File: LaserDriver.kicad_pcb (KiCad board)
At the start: 2 copper layers, 40.2 x 40.5 mm, 31 parts, among them J100 Screw_Terminal_01x04, J101 Screw_Terminal_01x02, J102 nano_left, J103 nano_right, U100 TPS92513DGQR

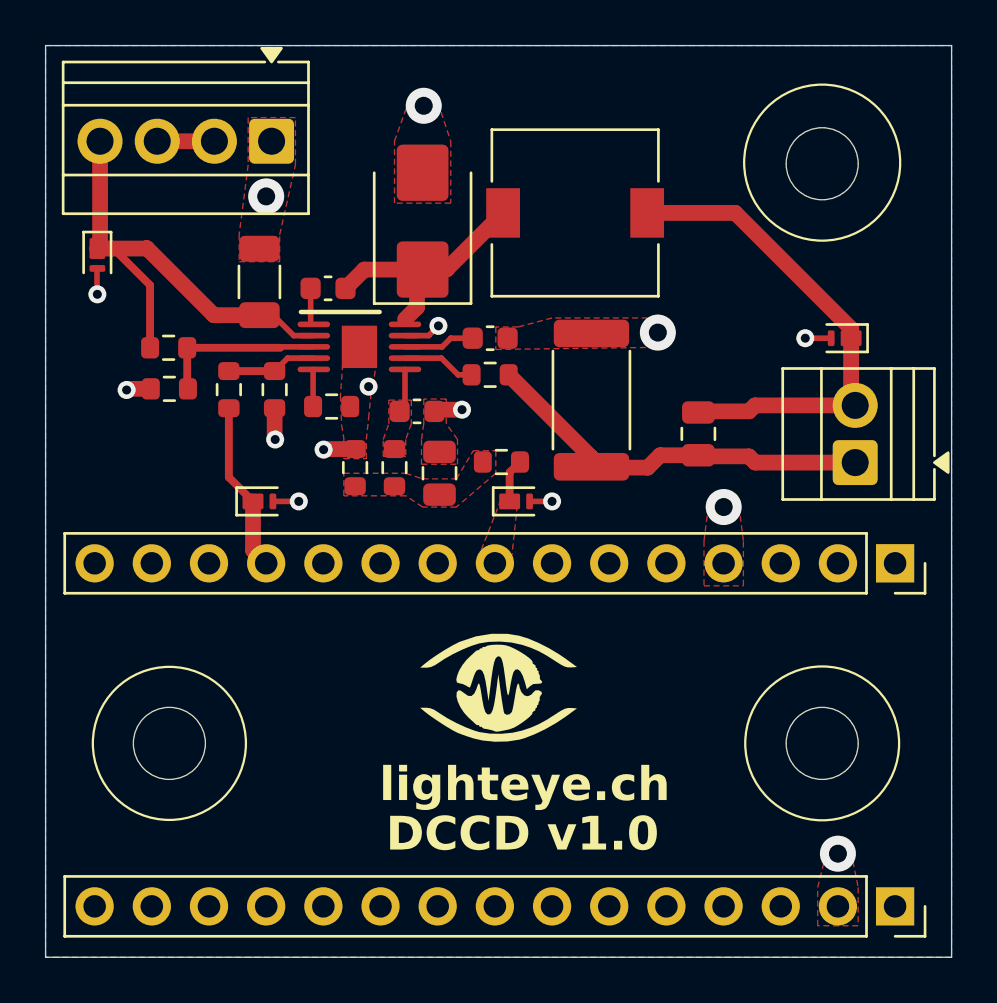
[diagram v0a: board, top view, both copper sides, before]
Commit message: increased screw size, fixed dimensions
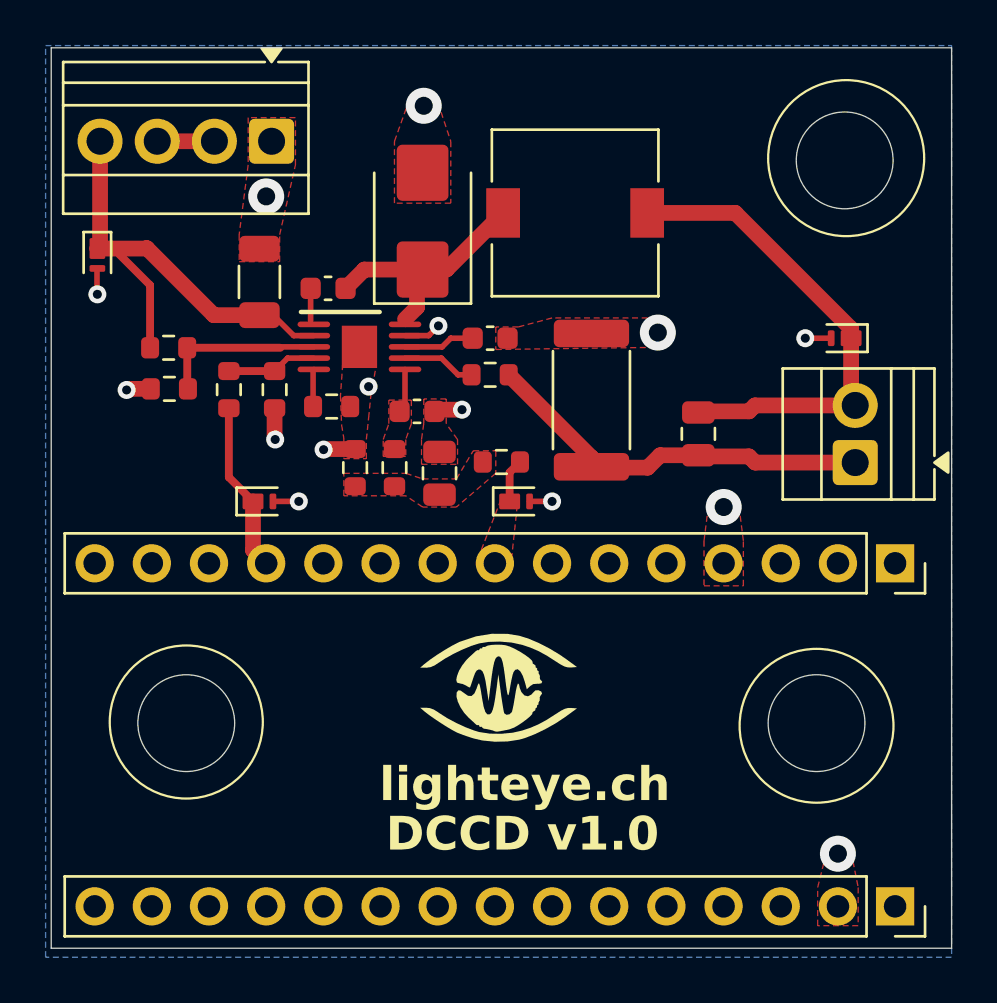
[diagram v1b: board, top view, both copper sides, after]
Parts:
- H1, H2, H3: footprint MountingHole:MountingHole_3.2mm_M3 -> MountingHole:MountingHole_4.3mm_M4
- moved H1 1.17 mm to (35.8, 127.1)
- moved H2 1.01 mm to (65.0, 102.1)
- moved H3 0.93 mm to (63.8, 127.1)
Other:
- board size 40.2 x 40.5 mm -> 40 x 40 mm

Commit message: fine changes
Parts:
- removed H2: MountingHole, MountingHole:MountingHole_4.3mm_M4
- moved J101 14.3 mm to (64.5, 101.3), turned to 180 degrees
- moved D102 10.1 mm to (58.5, 102.2), turned to -90 degrees
- moved C104 9.09 mm to (63.2, 106.5), turned to 0 degrees
- moved R105 2.06 mm to (55.8, 113.2), turned to -90 degrees
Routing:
- net Net-(D102-K): track 21.8 -> 12.8 mm
- net Net-(J101-Pin_1): track 18.1 -> 22.0 mm
- net GND: track 12.8 -> 13.9 mm
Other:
- board text added: "LightEye"
- board text removed: "lighteye.ch"

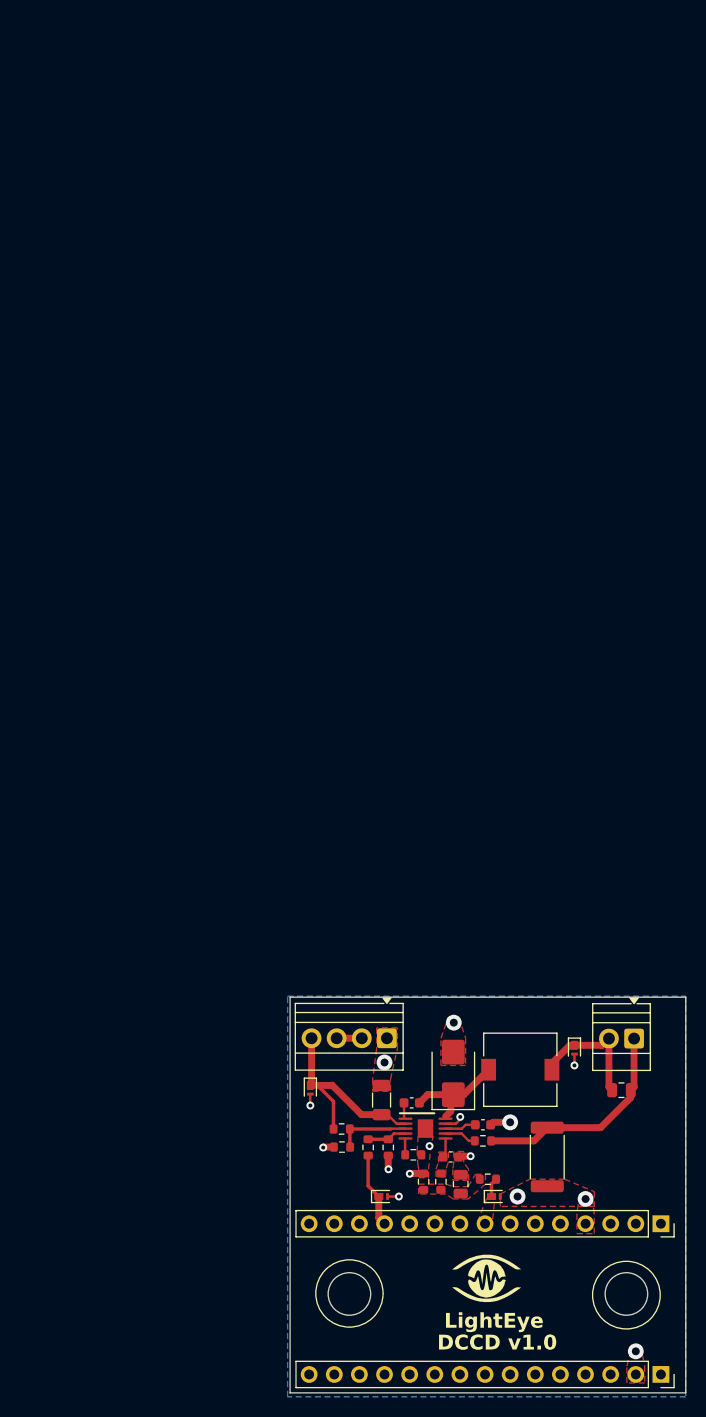
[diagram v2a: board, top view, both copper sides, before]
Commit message: Fixed supplier and manufacturer issues
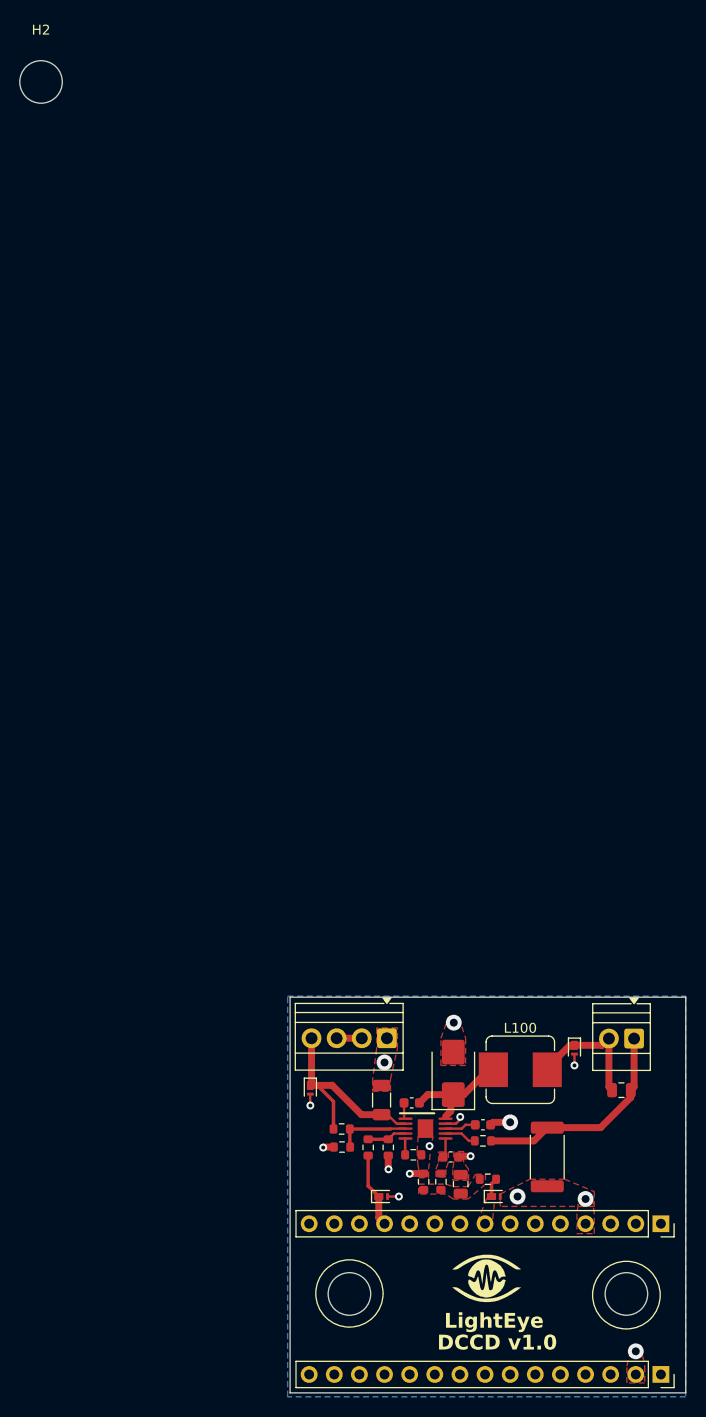
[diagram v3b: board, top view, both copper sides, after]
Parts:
- added H2: MountingHole, MountingHole:MountingHole_4.3mm_M4, F.Cu at (4.58, 4.58)
- L100: footprint Inductor_SMD:L_7.3x7.3_H4.5 -> Inductor_SMD:L_Bourns_SRP7028A_7.3x6.6mm
